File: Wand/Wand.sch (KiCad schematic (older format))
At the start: 29 parts, among them P1 ISP, P2 BASE, P3 EBS35, U1 OPA336N, U2 MPU-6050, U3 ATMEGA328-MMH, U4 TMP100, Y1 16MHz

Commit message: Another day, another 3.5mm Jack. This time just a basic panel mount one. The PCB mount ones are not going to fit in the required form factor.
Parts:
- removed R11: 2M, Resistors_SMD:R_0402, symbol R
- P3: value EBS35 -> KLB4; symbol REICHELT_EBS35 -> JACK_STEREO
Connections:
- net labels removed: TIP_DETECT
- wire segments 117 -> 113
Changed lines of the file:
@@
 LIBS:tmp10x
 LIBS:EBS35
+LIBS:JACK_STEREO
 LIBS:Wand-cache
 EELAYER 25 0
@@
 $EndComp
 $Comp
-L REICHELT_EBS35 P3
+L JACK_STEREO P3
 U 1 1 56411635
-P 10250 5100
-F 0 "P3" H 10250 5500 50  0000 C CNN
-F 1 "EBS35" H 10200 4800 50  0000 C CNN
-F 2 "Wand:Reichelt_EBS35" H 10350 4950 60  0001 C CNN
-F 3 "" H 10350 4950 60  0000 C CNN
-	1    10250 5100
-	1    0    0    -1
+P 10000 5000
+F 0 "P3" H 10000 5250 50  0000 C CNN
+F 1 "KLB4" H 9950 4700 50  0000 C CNN
+F 2 "Wand:Reichelt_EBS35" H 10100 4850 60  0001 C CNN
+F 3 "" H 10100 4850 60  0000 C CNN
+	1    10000 5000
+	-1   0    0    -1
 $EndComp
 $Comp
@@
 L GND #PWR06
 U 1 1 56416557
-P 9350 5050
-F 0 "#PWR06" H 9350 4800 50  0001 C CNN
-F 1 "GND" H 9350 4900 50  0000 C CNN
-F 2 "" H 9350 5050 60  0000 C CNN
-F 3 "" H 9350 5050 60  0000 C CNN
-	1    9350 5050
-	0    1    1    0
-$EndComp
-Text Label 9450 4950 2    60   ~ 0
+P 9350 5150
+F 0 "#PWR06" H 9350 4900 50  0001 C CNN
+F 1 "GND" H 9350 5000 50  0000 C CNN
+F 2 "" H 9350 5150 60  0000 C CNN
+F 3 "" H 9350 5150 60  0000 C CNN
+	1    9350 5150
+	1    0    0    -1
+$EndComp
+Text Label 9450 5050 2    60   ~ 0
 SENS
 Text Label 9450 4850 2    60   ~ 0
@@
 	-1   0    0    1
 $EndComp
-NoConn ~ 9650 5300
 $Comp
 L +3.3V #PWR011
@@
 	1    0    0    -1
 $EndComp
-Text Label 9350 5350 2    60   ~ 0
-TIP_DETECT
-$Comp
-L R R11
-U 1 1 564A6CD4
-P 9450 5200
-F 0 "R11" V 9530 5200 50  0000 C CNN
-F 1 "2M" V 9450 5200 50  0000 C CNN
-F 2 "Resistors_SMD:R_0402" V 9380 5200 30  0001 C CNN
-F 3 "" H 9450 5200 30  0000 C CNN
-	1    9450 5200
-	1    0    0    -1
-$EndComp
 Wire Wire Line
 	5950 5150 5950 5050
@@
 	9650 4850 9450 4850
 Wire Wire Line
-	9450 4950 9650 4950
+	9450 5050 9650 5050
 Wire Wire Line
 	1400 3650 1550 3650
@@
 Text Notes 8700 5850 0    60   ~ 0
 SENS pulled high (3.3v) with 1M resister
-Text Label 3600 1450 0    60   ~ 0
-TIP_DETECT
-Wire Wire Line
-	3450 1450 3600 1450
 Wire Wire Line
 	3450 3350 3600 3350
@@
 	1400 3650 1400 3900
 Wire Wire Line
-	9350 5350 9600 5350
-Wire Wire Line
-	9600 5350 9600 5200
-Wire Wire Line
-	9600 5200 9650 5200
-Connection ~ 9450 5350
-Wire Wire Line
-	9350 5050 9650 5050
-Connection ~ 9450 5050
+	9350 5150 9650 5150
+NoConn ~ 3450 1450
 $EndSCHEMATC

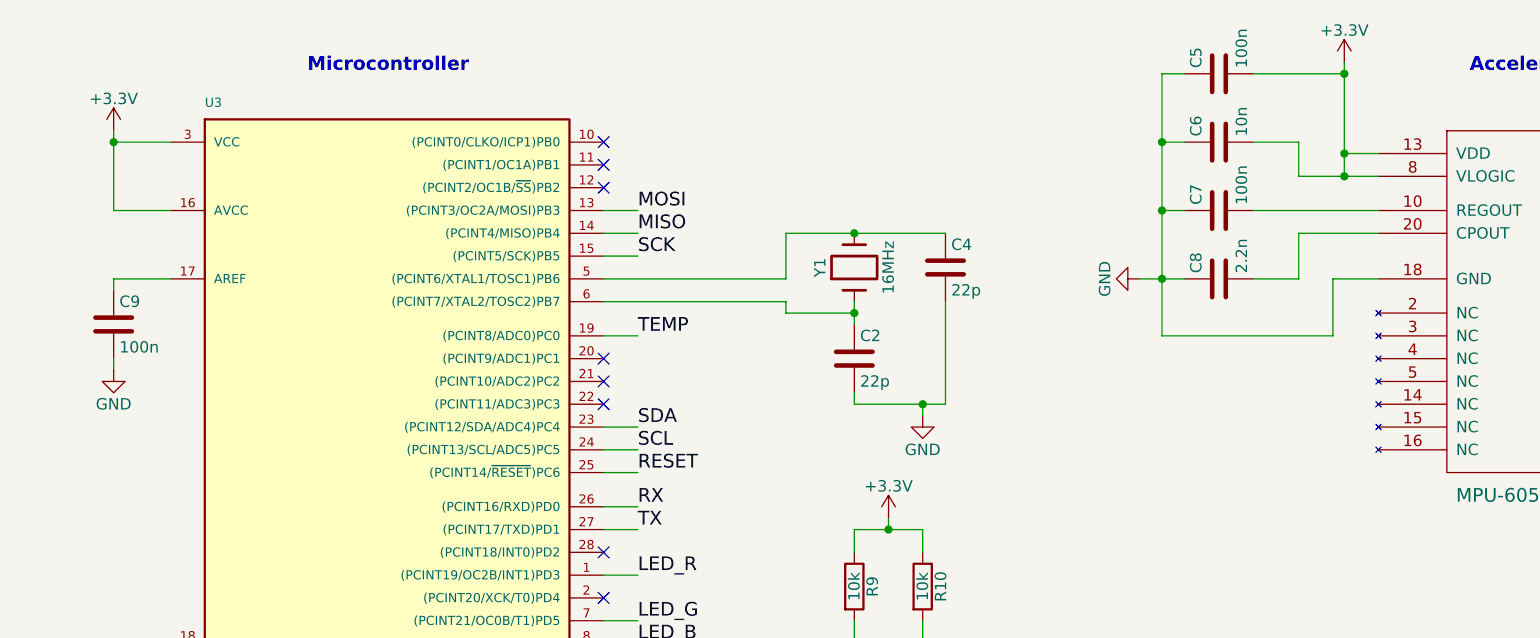
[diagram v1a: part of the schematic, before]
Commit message: Removed the crystal and took a few changes to match the RFm69Pi module from Open Energy Monitor as that works with Serial and no crystal.
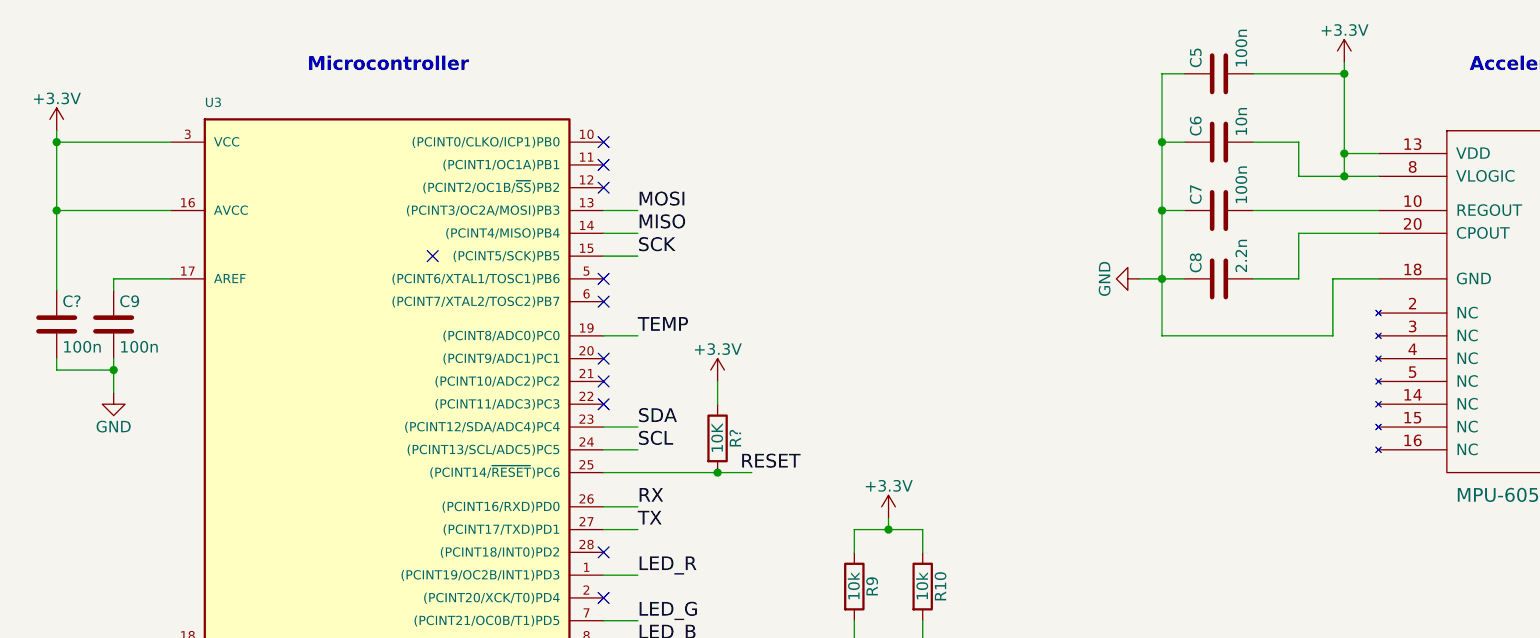
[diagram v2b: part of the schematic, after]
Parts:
- removed C2, C4: 22p, Capacitors_SMD:C_0402, symbol C
- removed Y1: 16MHz, symbol Crystal
- added C?: 100n, symbol C
- added R?: 10K, symbol R
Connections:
- net +3V3: now also C?.1, R?.1
- net GND: now also C?.2
- net RESET: now also R?.2
- no-connect marks 12 -> 15
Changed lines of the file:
@@
 $EndDescr
-$Comp
-L Crystal Y1
-U 1 1 563E76C3
-P 4550 2000
-F 0 "Y1" H 4550 2150 50  0000 C CNN
-F 1 "16MHz" H 4550 1850 50  0000 C CNN
-F 2 "" H 4550 2000 60  0001 C CNN
-F 3 "" H 4550 2000 60  0000 C CNN
-	1    4550 2000
-	0    -1   -1   0
-$EndComp
-$Comp
-L C C4
-U 1 1 563E774E
-P 4950 2000
-F 0 "C4" H 4975 2100 50  0000 L CNN
-F 1 "22p" H 4975 1900 50  0000 L CNN
-F 2 "Capacitors_SMD:C_0402" H 4988 1850 30  0001 C CNN
-F 3 "" H 4950 2000 60  0000 C CNN
-	1    4950 2000
-	1    0    0    -1
-$EndComp
-$Comp
-L C C2
-U 1 1 563E77D7
-P 4550 2400
-F 0 "C2" H 4575 2500 50  0000 L CNN
-F 1 "22p" H 4575 2300 50  0000 L CNN
-F 2 "Capacitors_SMD:C_0402" H 4588 2250 30  0001 C CNN
-F 3 "" H 4550 2400 60  0000 C CNN
-	1    4550 2400
-	1    0    0    -1
-$EndComp
 $Comp
 L R R8
@@
 Text Label 3600 2300 0    60   ~ 0
 TEMP
-$Comp
-L GND #PWR04
-U 1 1 56415081
-P 4850 2650
-F 0 "#PWR04" H 4850 2400 50  0001 C CNN
-F 1 "GND" H 4850 2500 50  0000 C CNN
-F 2 "" H 4850 2650 60  0000 C CNN
-F 3 "" H 4850 2650 60  0000 C CNN
-	1    4850 2650
-	1    0    0    -1
-$EndComp
 $Comp
 L GND #PWR05
@@
 Text Label 3600 1950 0    60   ~ 0
 SCK
-Text Label 3600 2900 0    60   ~ 0
+Text Label 4050 2900 0    60   ~ 0
 RESET
 Text Label 3600 3350 0    60   ~ 0
@@
 L +3.3V #PWR013
 U 1 1 5647BAD5
-P 1300 1400
-F 0 "#PWR013" H 1300 1250 50  0001 C CNN
-F 1 "+3.3V" H 1300 1540 50  0000 C CNN
-F 2 "" H 1300 1400 60  0000 C CNN
-F 3 "" H 1300 1400 60  0000 C CNN
-	1    1300 1400
+P 1050 1400
+F 0 "#PWR013" H 1050 1250 50  0001 C CNN
+F 1 "+3.3V" H 1050 1540 50  0000 C CNN
+F 2 "" H 1050 1400 60  0000 C CNN
+F 3 "" H 1050 1400 60  0000 C CNN
+	1    1050 1400
 	1    0    0    -1
 $EndComp
@@
 	6300 1150 6700 1150
 Wire Wire Line
-	6650 2300 5900 2300
-Wire Wire Line
-	6650 2050 6650 2300
-Wire Wire Line
-	6850 2050 6650 2050
+	5900 2300 6650 2300
+Wire Wire Line
+	6650 2300 6650 2050
+Wire Wire Line
+	6650 2050 6850 2050
 Wire Wire Line
 	6500 2050 6500 1850
@@
 	6500 1600 6500 1450
 Wire Wire Line
-	6850 1600 6500 1600
+	6500 1600 6850 1600
 Connection ~ 5900 1750
 Wire Wire Line
@@
 	5800 2050 6000 2050
 Wire Wire Line
-	5900 2300 5900 1150
+	5900 1150 5900 2300
 Wire Wire Line
 	6000 1750 5900 1750
@@
 	1300 2050 1550 2050
 Wire Wire Line
-	1300 1750 1550 1750
+	1050 1750 1550 1750
 Wire Wire Line
 	3600 1750 3450 1750
@@
 	3600 1950 3450 1950
 Wire Wire Line
-	3450 2900 3600 2900
+	3450 2900 4100 2900
 Wire Wire Line
 	3450 2700 3600 2700
@@
 Wire Wire Line
 	1400 3750 1550 3750
-Connection ~ 1300 1450
-Wire Wire Line
-	1300 1450 1550 1450
-Connection ~ 4850 2600
-Wire Wire Line
-	4550 2550 4550 2600
-Wire Wire Line
-	4850 2600 4850 2650
-Wire Wire Line
-	4550 2600 4950 2600
-Wire Wire Line
-	4950 2600 4950 2150
-Connection ~ 4550 2200
-Wire Wire Line
-	4250 2150 3450 2150
-Wire Wire Line
-	4250 2200 4250 2150
-Wire Wire Line
-	4550 2200 4250 2200
-Connection ~ 4550 1850
-Wire Wire Line
-	4550 2150 4550 2250
-Wire Wire Line
-	4250 1850 4950 1850
-Wire Wire Line
-	4250 2050 4250 1850
-Wire Wire Line
-	3450 2050 4250 2050
+Connection ~ 1050 1450
+Wire Wire Line
+	1050 1450 1550 1450
 Wire Wire Line
 	3450 2300 3600 2300
@@
 Cold junction temp
 Wire Wire Line
-	1300 1400 1300 1750
+	1050 1400 1050 2100
 $Comp
 L C C9
@@
 L GND #PWR024
 U 1 1 564C6A3E
-P 1300 2450
-F 0 "#PWR024" H 1300 2200 50  0001 C CNN
-F 1 "GND" H 1300 2300 50  0000 C CNN
-F 2 "" H 1300 2450 60  0000 C CNN
-F 3 "" H 1300 2450 60  0000 C CNN
-	1    1300 2450
-	1    0    0    -1
-$EndComp
-Wire Wire Line
-	1300 2400 1300 2450
+P 1300 2550
+F 0 "#PWR024" H 1300 2300 50  0001 C CNN
+F 1 "GND" H 1300 2400 50  0000 C CNN
+F 2 "" H 1300 2550 60  0000 C CNN
+F 3 "" H 1300 2550 60  0000 C CNN
+	1    1300 2550
+	1    0    0    -1
+$EndComp
 Wire Wire Line
 	1300 2050 1300 2100
@@
 	9350 5150 9650 5150
 NoConn ~ 3450 1450
+NoConn ~ 3450 2050
+NoConn ~ 3450 2150
+NoConn ~ 2700 1950
+$Comp
+L R R?
+U 1 1 56959728
+P 3950 2750
+F 0 "R?" V 4030 2750 50  0000 C CNN
+F 1 "10K" V 3950 2750 50  0000 C CNN
+F 2 "" V 3880 2750 50  0000 C CNN
+F 3 "" H 3950 2750 50  0000 C CNN
+	1    3950 2750
+	1    0    0    -1
+$EndComp
+$Comp
+L +3.3V #PWR?
+U 1 1 56959787
+P 3950 2500
+F 0 "#PWR?" H 3950 2350 50  0001 C CNN
+F 1 "+3.3V" H 3950 2640 50  0000 C CNN
+F 2 "" H 3950 2500 50  0000 C CNN
+F 3 "" H 3950 2500 50  0000 C CNN
+	1    3950 2500
+	1    0    0    -1
+$EndComp
+Connection ~ 3950 2900
+Wire Wire Line
+	3950 2500 3950 2600
+$Comp
+L C C?
+U 1 1 56959BA2
+P 1050 2250
+F 0 "C?" H 1075 2350 50  0000 L CNN
+F 1 "100n" H 1075 2150 50  0000 L CNN
+F 2 "" H 1088 2100 50  0000 C CNN
+F 3 "" H 1050 2250 50  0000 C CNN
+	1    1050 2250
+	1    0    0    -1
+$EndComp
+Connection ~ 1050 1750
+Wire Wire Line
+	1300 2400 1300 2550
+Wire Wire Line
+	1050 2400 1050 2450
+Wire Wire Line
+	1050 2450 1300 2450
+Connection ~ 1300 2450
 $EndSCHEMATC

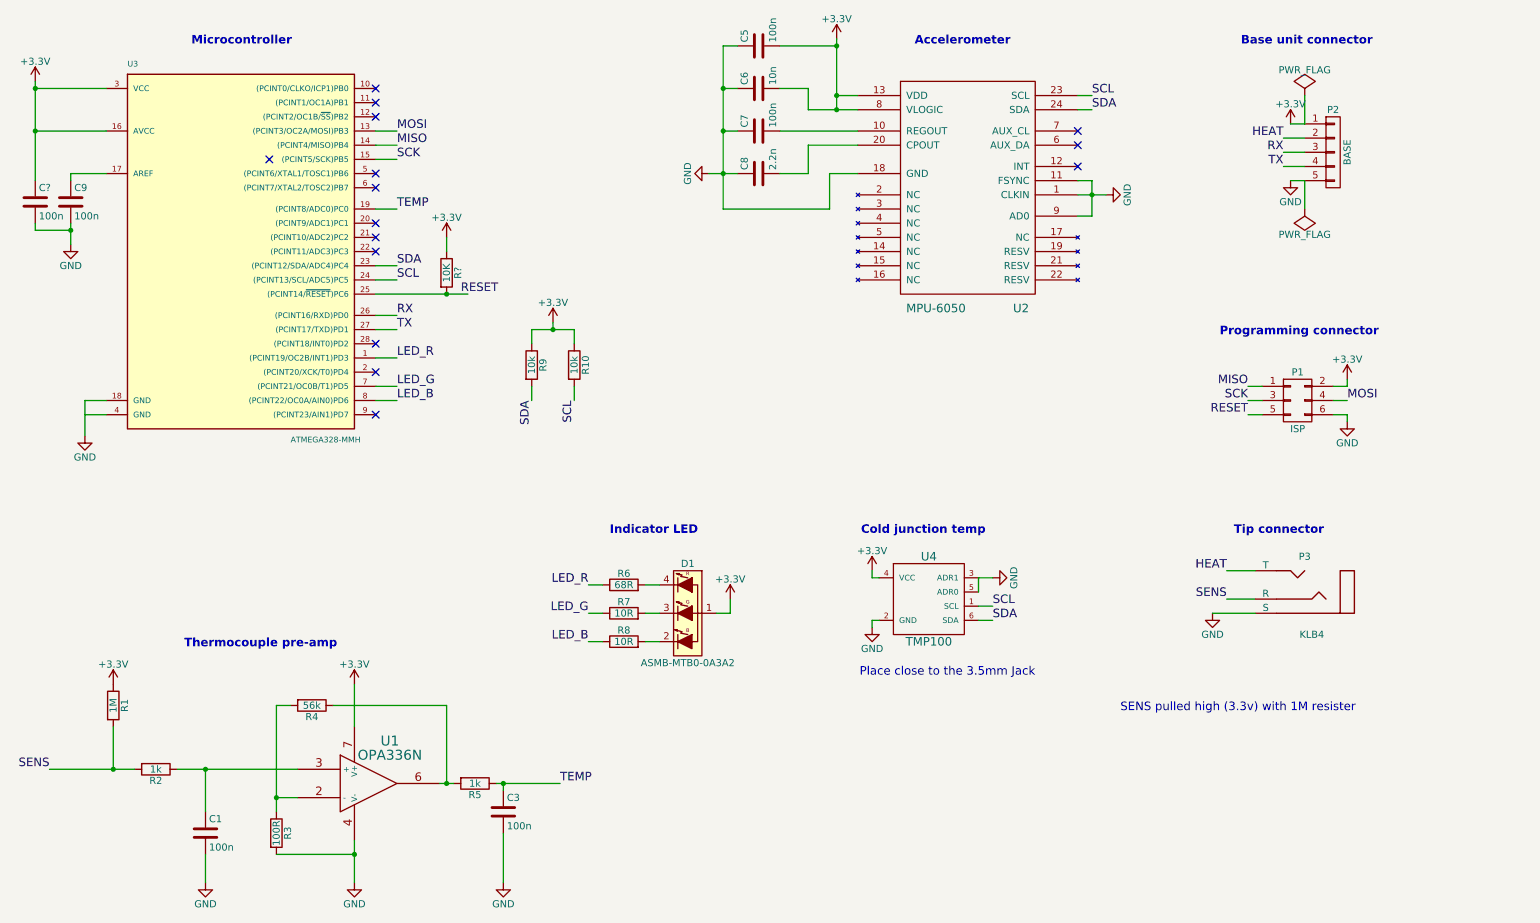
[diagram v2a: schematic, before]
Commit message: Changed over to using the MAX31855 for reading the temperature to reduce the component count and also make virtually all the wand digital signals
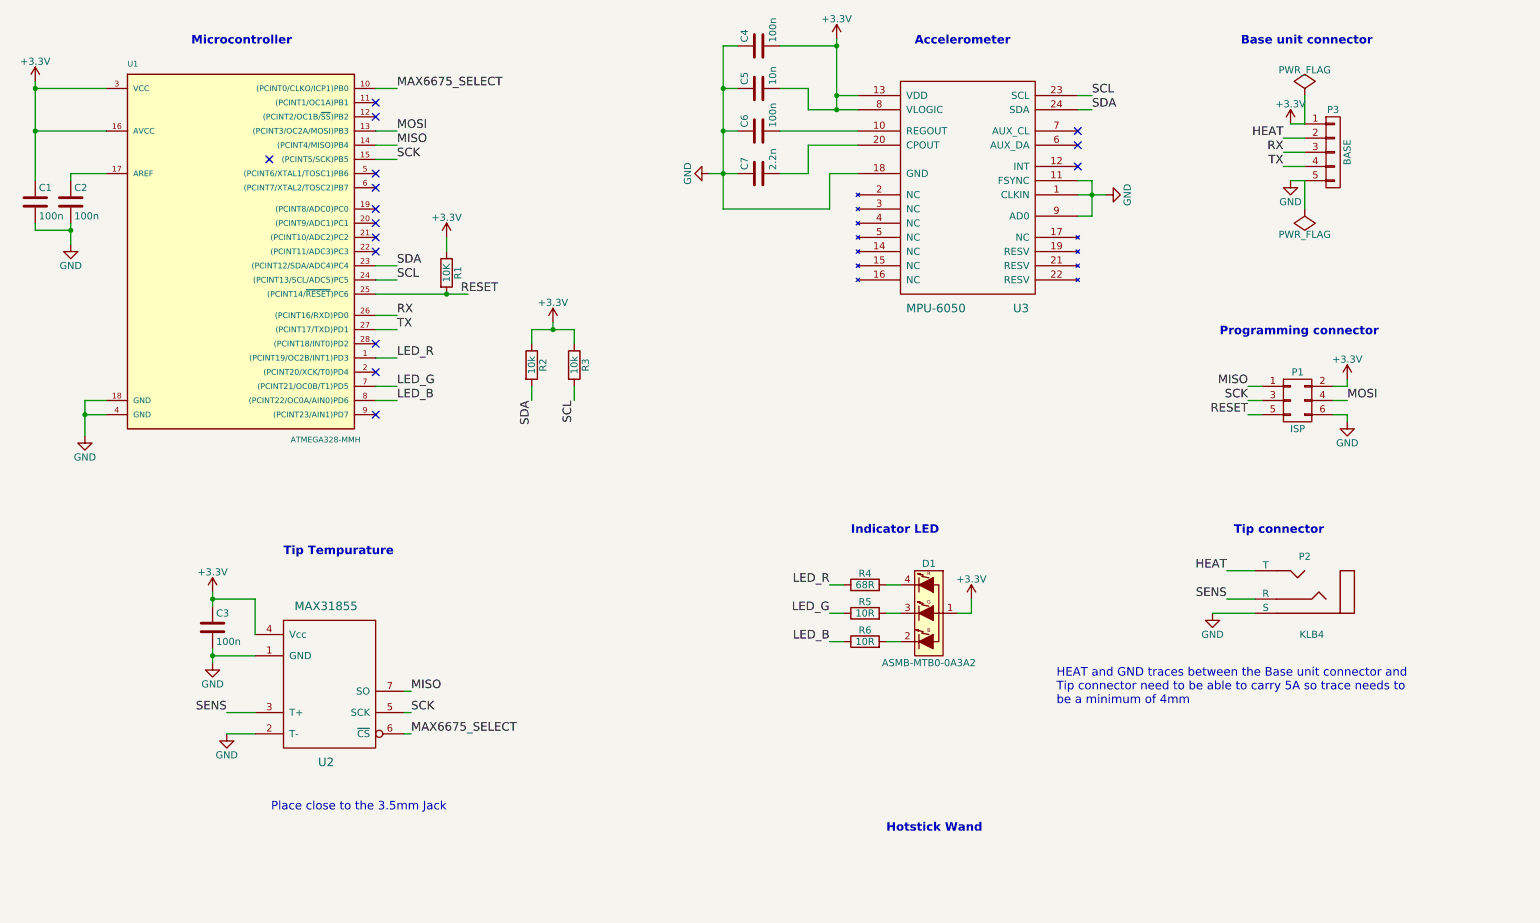
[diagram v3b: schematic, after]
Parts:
- removed C1: 100n, Capacitors_SMD:C_0402, symbol C
- removed R1: 1M, Resistors_SMD:R_0402, symbol R
- removed R2, R5: 1k, Resistors_SMD:R_0402, symbol R
- removed R3: 100R, Resistors_SMD:R_0402, symbol R
- removed R4: 56k, Resistors_SMD:R_0402, symbol R
- removed U1: OPA336N, Wand:OPA336_Plastic_Small, symbol TL071-RESCUE-Wand
- removed U4: TMP100, TO_SOT_Packages_SMD:SOT-23-6, symbol TMP100
- added U2: MAX31855, Housings_SOIC:SOIC-8_3.9x4.9mm_Pitch1.27mm, symbol MAX6675
- C1: renamed from C?; footprint (none) -> Capacitors_SMD:C_0402
- R1: renamed from R?; footprint (none) -> Resistors_SMD:R_0402
- renumbered C9 to C2, C5 to C4, C6 to C5, C7 to C6, C8 to C7, P3 to P2, P2 to P3, R9 to R2, R10 to R3, R6 to R4, R7 to R5, R8 to R6, U3 to U1, U2 to U3
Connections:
- net +3V3: now also C3.1, U2.4 (Vcc)
- net GND: now also U1.4 (GND), U2.1 (GND), U2.2 (T-)
- net MISO: now also U2.7 (SO)
- net SCK: now also U2.5 (SCK)
- net SENS: now also U2.3 (T+)
- net MAX6675_SELECT: now reaches U1.10 ((PCINT0/CLKO/ICP1)PB0)
- net MAX6675_SELECT: now also U2.6 (~CS)
- net TEMP: no longer names the net of U1.19 ((PCINT8/ADC0)PC0)
- net TEMP: no longer C3.1
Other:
- note added: "HEAT and GND traces between the Base unit connector and \nTip connector need to be able to carry 5A so trace needs to \nbe a minimum of 4mm"
- note added: "Hotstick Wand"
- note added: "Tip Tempurature"
- note removed: "Cold junction temp"
- note removed: "SENS pulled high (3.3v) with 1M resister"
- note removed: "Thermocouple pre-amp"
- moved on the sheet: D1, R4, R5, R6

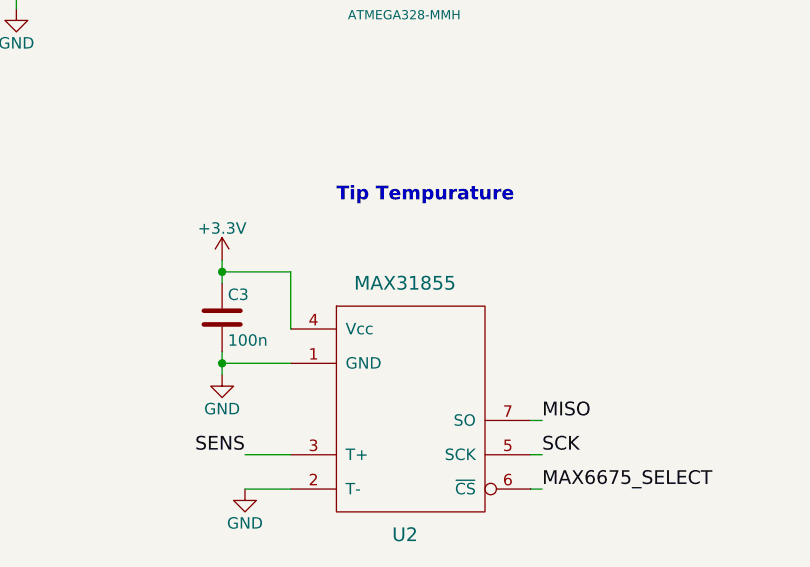
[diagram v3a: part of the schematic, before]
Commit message: Exact part number for the Tip temp sensor
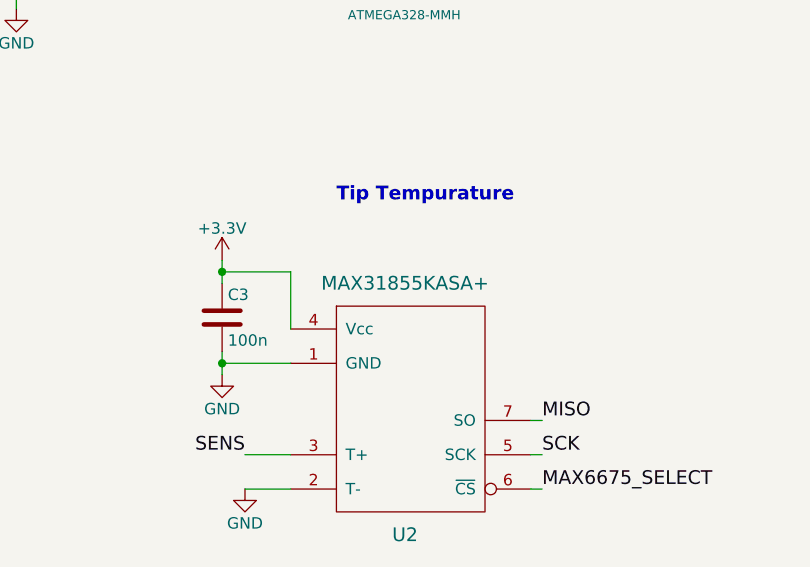
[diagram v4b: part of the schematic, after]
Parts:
- U2: value MAX31855 -> MAX31855KASA+
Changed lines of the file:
@@
 P 3100 5650
 F 0 "U2" H 3100 5100 60  0000 C CNN
-F 1 "MAX31855" H 3100 6200 60  0000 C CNN
+F 1 "MAX31855KASA+" H 3100 6200 60  0000 C CNN
 F 2 "Housings_SOIC:SOIC-8_3.9x4.9mm_Pitch1.27mm" H 3050 5700 60  0001 C CNN
 F 3 "" H 3050 5700 60  0000 C CNN
